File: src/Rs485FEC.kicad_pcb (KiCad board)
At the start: 2 copper layers, 24 x 27.9 mm, 21 parts, among them J1 B4B-XH-A, P1 105444-0001, Q1 DMP3099L-13, U1 FT232RL, U2 SP485E

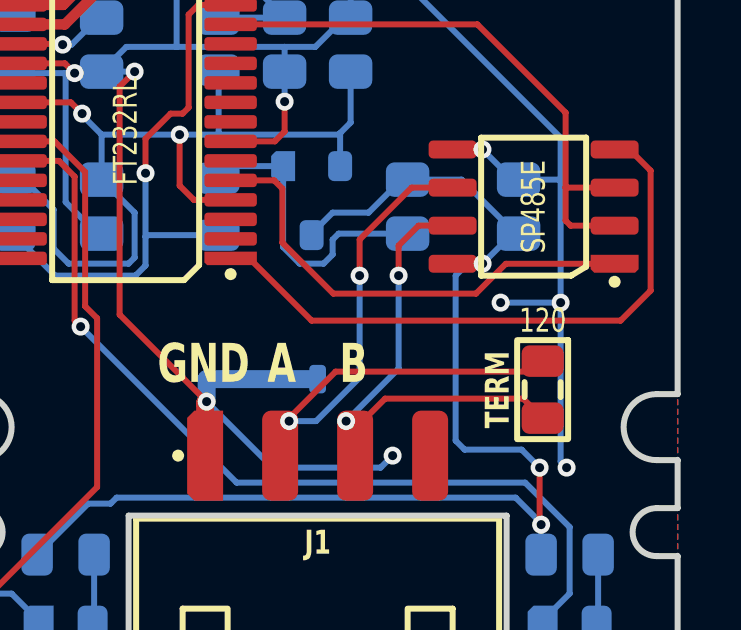
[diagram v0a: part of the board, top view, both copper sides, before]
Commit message: Refactoring copper pour
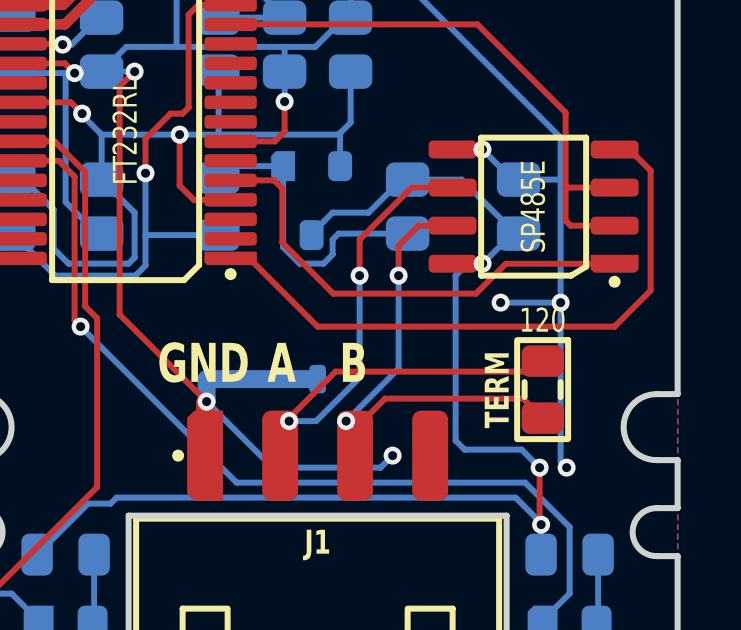
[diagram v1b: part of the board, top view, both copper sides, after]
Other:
- rule pad_to_mask_clearance: 0 -> 0.05
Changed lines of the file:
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@@
       (dielectric_constraints no)
     )
-    (pad_to_mask_clearance 0)
+    (pad_to_mask_clearance 0.05)
     (aux_axis_origin 20 20)
     (pcbplotparams
@@
         (effects (font (size 0.8 0.6) (thickness 0.15)) (justify mirror))
     )
+    (fp_text user "D" (at 0 0.5) (layer "Cmts.User" knockout)
+        (effects (font (size 0.13 0.07) (thickness 0.01) bold))
+    )
     (fp_text user "S" (at 0.95 -0.5) (layer "Cmts.User" knockout)
         (effects (font (size 0.13 0.07) (thickness 0.01) bold))
     )
     (fp_text user "G" (at -0.95 -0.5) (layer "Cmts.User" knockout)
-        (effects (font (size 0.13 0.07) (thickness 0.01) bold))
-    )
-    (fp_text user "D" (at 0 0.5) (layer "Cmts.User" knockout)
         (effects (font (size 0.13 0.07) (thickness 0.01) bold))
     )
     (fp_rect (start -1.35 0.25) (end 1.35 -0.25)
       (stroke (width 0.2) (type default)) (fill none) (layer "B.SilkS"))
-    (fp_circle (center -1.575 -1.15) (end -1.425 -1.15)
+    (fp_circle (center -1.65 -1.15) (end -1.5 -1.15)
       (stroke (width 0.1) (type solid)) (fill solid) (layer "B.SilkS"))
     (fp_rect (start -1.75 1.95) (end 1.75 -1.95)
@@
   (via (at 21.9 23.8) (size 0.6) (drill 0.3) (layers "F.Cu" "B.Cu") (net 1))
   (segment (start 21.9 23.8) (end 21.9 26.13) (width 0.2) (layer "B.Cu") (net 1))
-  (segment (start 31.8 36.3) (end 29.725 34.225) (width 0.2) (layer "F.Cu") (net 2))
-  (segment (start 42.1 36.3) (end 31.8 36.3) (width 0.2) (layer "F.Cu") (net 2))
-  (segment (start 43.1 35.3) (end 42.1 36.3) (width 0.2) (layer "F.Cu") (net 2))
   (segment (start 42.395343 30.595) (end 43.1 31.299657) (width 0.2) (layer "F.Cu") (net 2))
+  (segment (start 43.1 35.3) (end 41.9 36.5) (width 0.2) (layer "F.Cu") (net 2))
   (segment (start 43.1 31.299657) (end 43.1 35.3) (width 0.2) (layer "F.Cu") (net 2))
+  (segment (start 32 36.5) (end 29.725 34.225) (width 0.2) (layer "F.Cu") (net 2))
+  (segment (start 41.9 36.5) (end 32 36.5) (width 0.2) (layer "F.Cu") (net 2))
   (segment (start 27.875 32.275) (end 27.4 31.8) (width 0.2) (layer "F.Cu") (net 3))
   (segment (start 29.1 32.275) (end 27.875 32.275) (width 0.2) (layer "F.Cu") (net 3))
@@
   (segment (start 32.6 38) (end 39.15 38) (width 0.2) (layer "F.Cu") (net 17))
   (segment (start 36.5 31.865) (end 35.135 31.865) (width 0.2) (layer "F.Cu") (net 17))
-  (segment (start 39.15 38) (end 39.5 37.65) (width 0.2) (layer "F.Cu") (net 17))
   (via (at 31.049975 39.65) (size 0.6) (drill 0.3) (layers "F.Cu" "B.Cu") (net 17))
   (via (at 33.4 34.8) (size 0.6) (drill 0.3) (layers "F.Cu" "B.Cu") (net 17))
@@
   (segment (start 40.435 33.135) (end 40.265 32.965) (width 0.2) (layer "F.Cu") (net 19))
   (zone (net 7) (net_name "GND") (layers "F&B.Cu") (hatch edge 0.5)
-    (connect_pads (clearance 0.2))
-    (min_thickness 0.2) (filled_areas_thickness no)
+    (connect_pads no (clearance 0.3))
+    (min_thickness 0.3) (filled_areas_thickness no)
     (fill yes (thermal_gap 0.5) (thermal_bridge_width 0.5))
     (polygon
